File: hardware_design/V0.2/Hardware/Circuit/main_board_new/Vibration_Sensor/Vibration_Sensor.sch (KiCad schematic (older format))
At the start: 14 parts

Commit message: New PCB design
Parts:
- removed C?: C, symbol Device:C
- removed R? (x3): R, symbol Device:R
- removed U?: nRF24L01+, symbol ARTS-Lab:nRF24L01+
- removed U?: INA219AxD, Package_SO:SOIC-8_3.9x4.9mm_P1.27mm, symbol Analog_ADC:INA219AxD
- added C1, C2, C3: C, Capacitor_SMD:C_1206_3216Metric_Pad1.33x1.80mm_HandSolder, symbol Device:C
- added U3, U4: AP7361C-33E, Package_TO_SOT_SMD:SOT-223-3_TabPin2, symbol Regulator_Linear:AP7361C-33E
- D1: renamed from D?; footprint (none) -> LED_THT:LED_D3.0mm
- F1: renamed from F?; footprint (none) -> Capacitor_SMD:C_1206_3216Metric_Pad1.33x1.80mm_HandSolder
- Micro_SD1: renamed from Micro_SD?; footprint (none) -> custom:small_microSD_v2
- R1: renamed from R?; footprint (none) -> Resistor_SMD:R_1206_3216Metric_Pad1.30x1.75mm_HandSolder
- U1: renamed from U?; footprint custom:XT60Github -> custom:XT60PW
- U2: renamed from U?; footprint (none) -> custom:Teensy40
- U5: renamed from U?; footprint (none) -> custom:top_rail
- switch1: renamed from switch?; footprint (none) -> custom:grounded_switch
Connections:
- net GND: now also C1.2, C2.2, C3.2, U3.2 (GND), U4.2 (GND)
- net at U2.33 (VIN): now also U5.7 (5V), C2.1, U3.3 (VO), U4.1 (VI)
- net at Micro_SD1.1 (3.3V), U5.8 (3.3V): now also C3.1, U4.3 (VO)
- net at switch1.2: now also C1.1, U3.1 (VI)

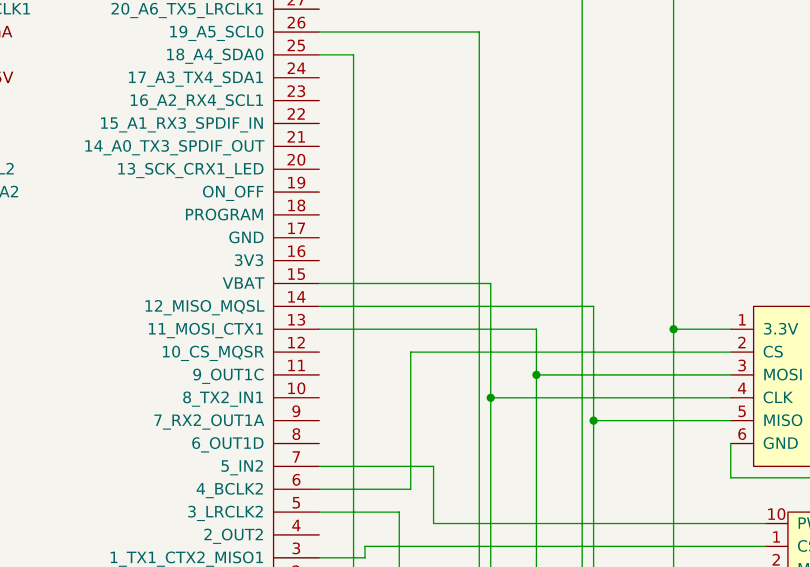
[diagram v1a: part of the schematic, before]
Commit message: Updated kicad and beam testing files
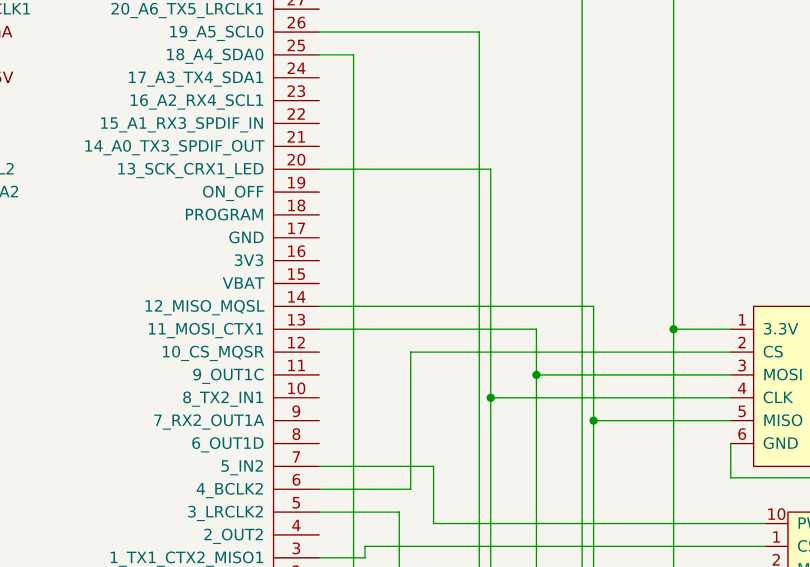
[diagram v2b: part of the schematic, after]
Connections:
- net at Micro_SD1.4 (CLK), U5.4 (SCK): now also U2.20 (13_SCK_CRX1_LED); no longer U2.15 (VBAT)
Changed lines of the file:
@@
 	6100 4400 5050 4400
-Wire Wire Line
-	5050 4400 5050 3900
-Wire Wire Line
-	5050 3900 4300 3900
 Wire Wire Line
 	6250 5350 5050 5350
@@
 Wire Wire Line
 	4650 1600 4650 1700
+Wire Wire Line
+	5050 3400 4300 3400
+Wire Wire Line
+	5050 3400 5050 4400
 $EndSCHEMATC
